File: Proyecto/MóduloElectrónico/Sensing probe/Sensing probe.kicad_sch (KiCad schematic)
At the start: 37 parts, among them J1 Conn_01x02, J2 Conn_01x02, J3 Conn_01x03_Pin, J4 Conn_01x02, J5 Conn_01x02, U1 CA3140, U2 LM324, U4 CA3140, U5 LM324

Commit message: Update sensing board
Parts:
- added D1: 1N4007, Diode_THT:D_DO-34_SOD68_P2.54mm_Vertical_AnodeUp, symbol Diode:1N4007
- added J6: Conn_01x03_Pin, Connector_PinHeader_2.54mm:PinHeader_1x03_P2.54mm_Vertical, symbol Connector:Conn_01x03_Pin
- added K1: HFD23, JohnsCustomLibrary:HFD23, symbol JohnsCustomLibrary:HFD23
- added Q1: Q_NPN_EBC, Package_TO_SOT_THT:TO-92, symbol Transistor_BJT:Q_NPN_EBC
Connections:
- net +5V: now also J6.1 (Pin_1), Q1.3 (C)
- net GND: now also D1.2 (A), J6.3 (Pin_3), K1.A2
- net TX: now reaches U3.16 (TX1)
- net TX: now also J6.2 (Pin_2)
- net RELAY: now reaches U3.25 (D7)
- net RELAY: now also Q1.2 (B)
- new net: D1.1 (K), K1.A1, Q1.1 (E)
- no-connect marks 34 -> 35
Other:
- moved on the sheet: U5B, U5C, U5D

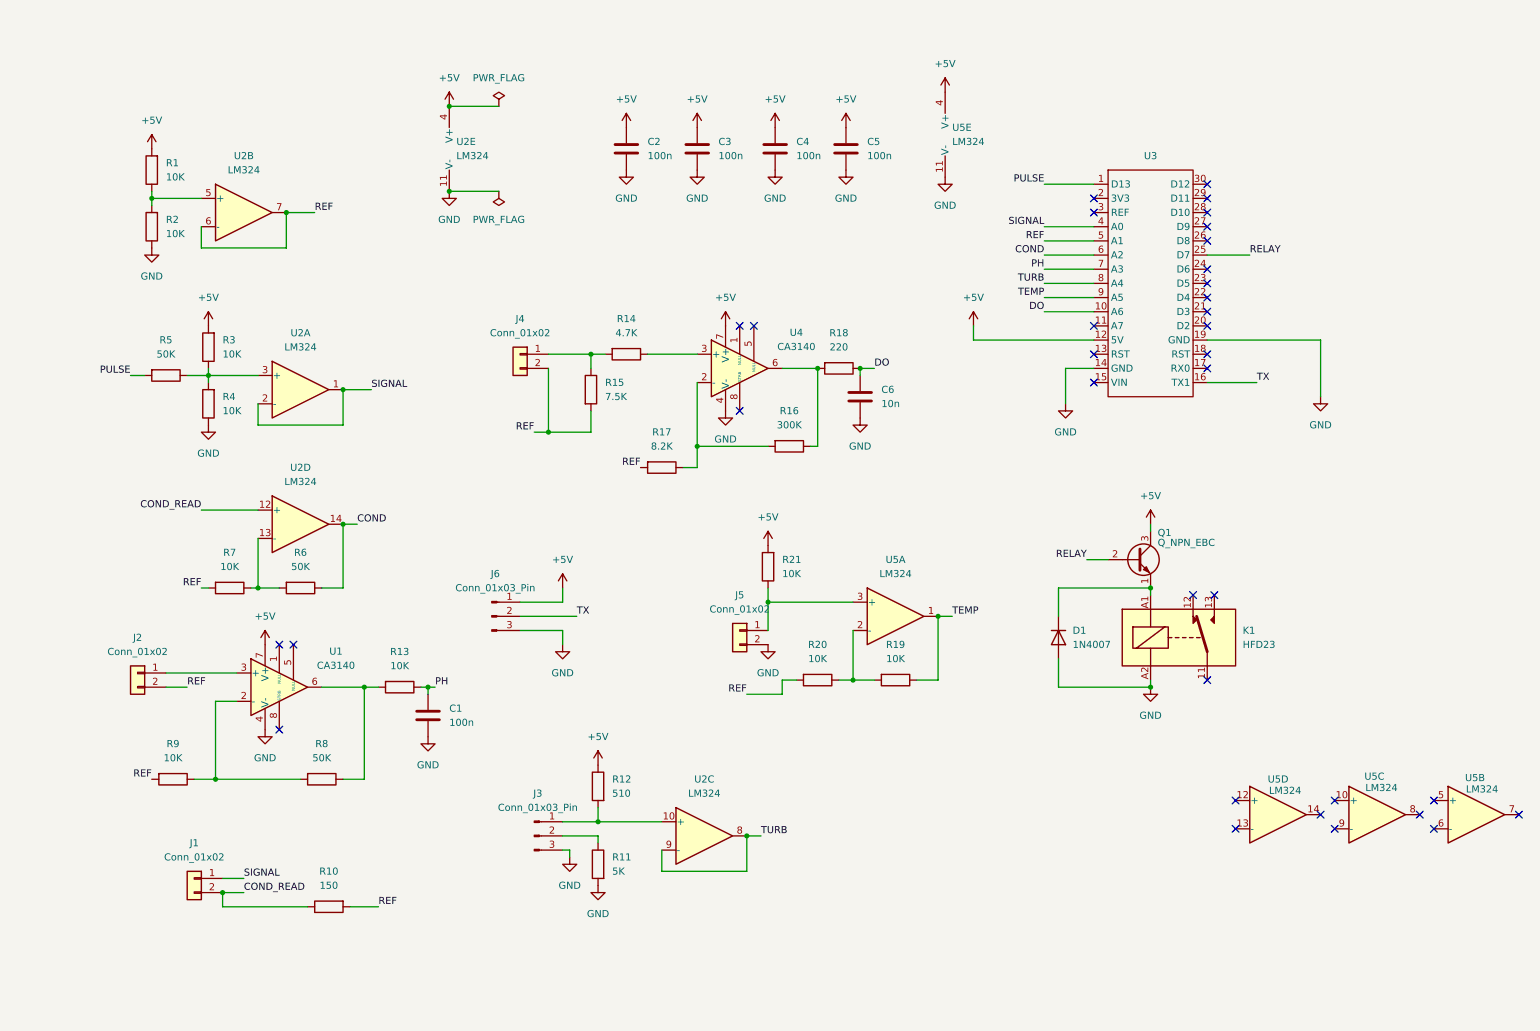
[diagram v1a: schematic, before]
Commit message: Desconector de sensor de conductividad
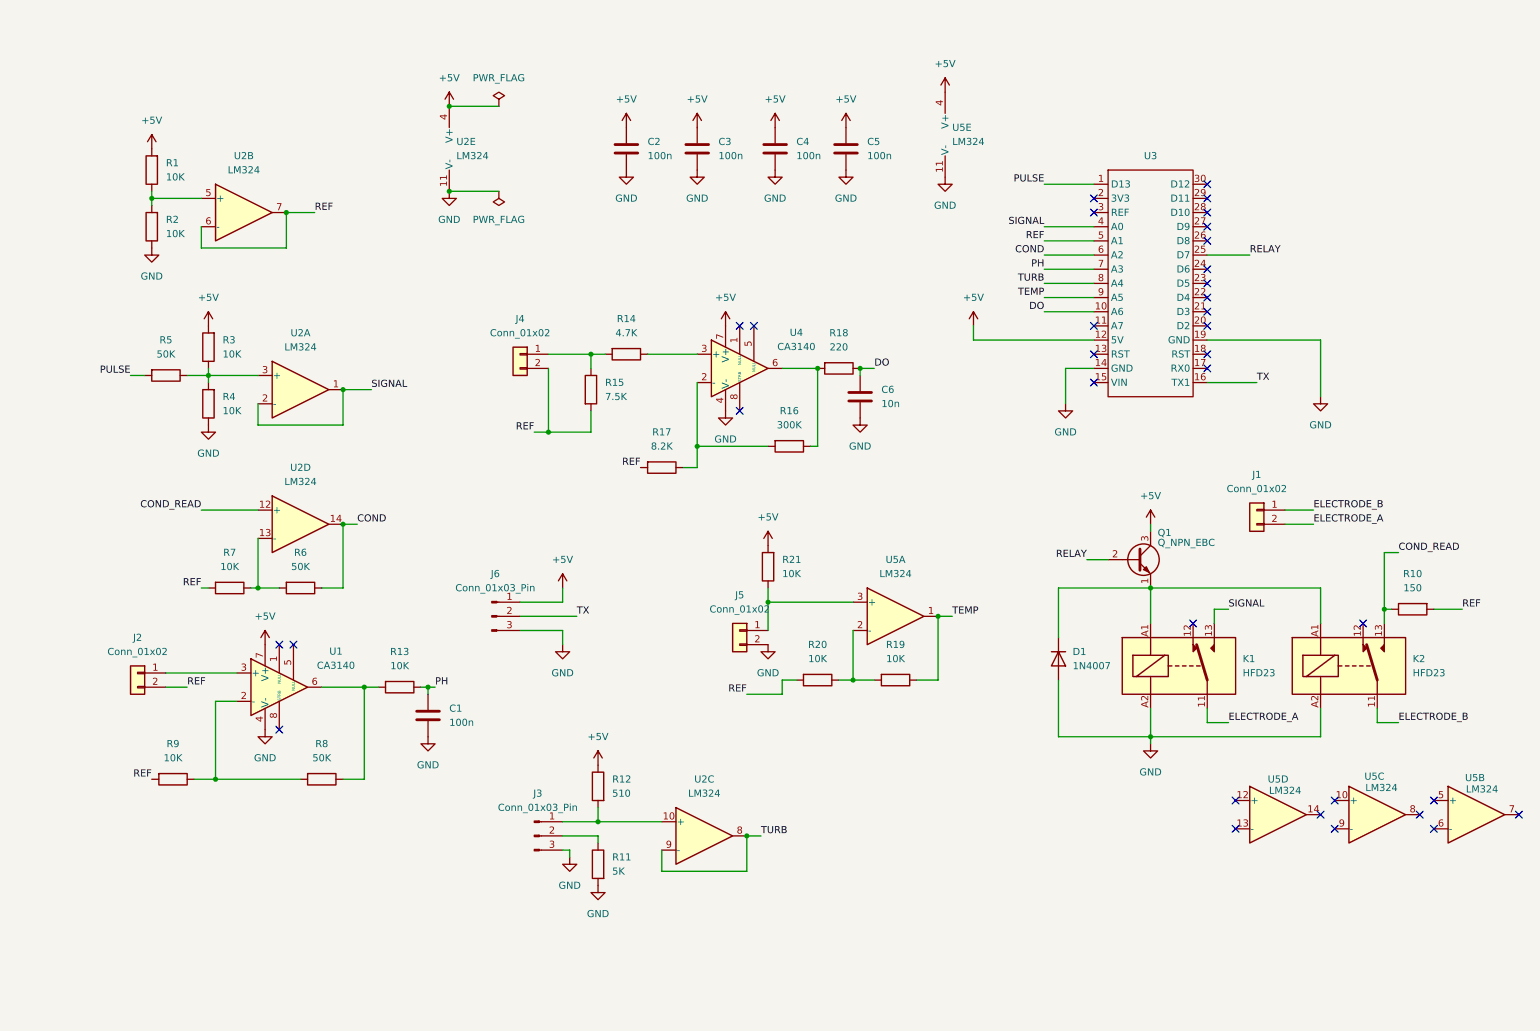
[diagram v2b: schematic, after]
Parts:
- added K2: HFD23, JohnsCustomLibrary:HFD23, symbol JohnsCustomLibrary:HFD23
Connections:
- net COND_READ: now also K2.13; no longer J1.2 (Pin_2)
- net GND: now also K2.A2
- net SIGNAL: now also K1.13; no longer J1.1 (Pin_1)
- net at D1.1 (K), K1.A1, Q1.1 (E): now also K2.A1
- net ELECTRODE_A: now reaches K1.11
- net ELECTRODE_A: now also J1.2 (Pin_2)
- new net ELECTRODE_B: J1.1 (Pin_1), K2.11
- no-connect marks 35 -> 34
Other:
- moved on the sheet: D1, J1, K1, R10

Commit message: Add files via upload
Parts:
- added D2: 1N4007, Diode_THT:D_DO-34_SOD68_P2.54mm_Vertical_AnodeUp, symbol Diode:1N4007
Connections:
- net GND: now also D2.2 (A)
- net at D1.1 (K), K1.A1, K2.A1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: now also D2.1 (K)
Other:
- note added: "ALIMENTACIÓN, DESACOPLADO Y COMUNICACIÓN"
- note added: "AMPLIFICADORES NO UTILIZADOS"
- note added: "CONTROLADOR"
- note added: "DEJAR ELECTRODOS FLOTANDO"
- note added: "GENERAR PULSO DE EXCITACIÓN"
- note added: "GENERAR VOLTAJE DE REFERENCIA"
- note added: "LEER SENSOR DE CONDUCTIVIDAD"
- note added: "LEER SENSOR DE OXÍGENO DISUELTO"
- note added: "LEER SENSOR DE PH"
- note added: "LEER SENSOR DE TEMPERATURA"
- note added: "LEER SENSOR DE TURBIDEZ"
- company: (none) -> Universidad Peruana Cayetano Heredia [UPCH]
- title: (none) -> Placa de sensado [Napduino]
- moved on the sheet: C1, C2, C3, C4, C5, C6, D1, J1, J2, J3, J4, J5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

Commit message: Branch alternativo
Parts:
- removed J5: Conn_01x02, Connector_PinHeader_2.54mm:PinHeader_1x02_P2.54mm_Vertical, symbol Connector_Generic:Conn_01x02
- added J5: Conn_01x03_Pin, Connector_PinHeader_2.54mm:PinHeader_1x03_P2.54mm_Vertical, symbol Connector:Conn_01x03_Pin
- added R22: 1K, Resistor_THT:R_Axial_DIN0204_L3.6mm_D1.6mm_P2.54mm_Vertical, symbol Device:R
- added R23: 10K, Resistor_THT:R_Axial_DIN0204_L3.6mm_D1.6mm_P2.54mm_Vertical, symbol Device:R
- added R24: 15K, Resistor_THT:R_Axial_DIN0204_L3.6mm_D1.6mm_P2.54mm_Vertical, symbol Device:R
- R2: value 10K -> 3.3K
- R20: value 10K -> 15K
- R5: value 50K -> 33K
- U3: footprint JohnsCustomLibrary:Arduino nano -> (none)
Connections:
- net +5V: now also J5.1 (Pin_1), R23.2; no longer R3.2
- net GND: now also R20.2, J5.3 (Pin_3), R22.1, R24.1; no longer R2.1
- net PULSE: now also R19.1; no longer R5.2
- net TEMP: now also R21.1, U3.23 (D5), J5.2 (Pin_2); no longer R19.1, U3.9 (A5), U5.1
- net at U5.3 (+): now also R19.2, R20.1; no longer R21.1
- net at U5.12 (+): now also R23.1, R24.2
- net 3V: now reaches U5.13 (-)
- net 3V: now also R3.2, U5.14
- net REF renamed 1.5V
- net 1.5V: no longer R20.2
- new net: R5.2, U5.1, U5.2 (-)
- new net: R2.1, R22.2
- no-connect marks 34 -> 31
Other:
- note added: "LEER TEMPERATURA"
- note added: "REFERENCIA 1.5V"
- note added: "REFERENCIA 3V"
- note removed: "GENERAR VOLTAJE DE REFERENCIA"
- note removed: "LEER SENSOR DE TEMPERATURA"
- moved on the sheet: C1, C2, C3, C4, C5, C6, J2, J3, J4, J6, R11, R12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
